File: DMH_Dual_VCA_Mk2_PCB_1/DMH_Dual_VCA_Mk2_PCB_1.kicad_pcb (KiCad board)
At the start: 2 copper layers, 48 x 175 mm, 70 parts, among them J1 TS_Jack_6.35mm_Sw, J100 IDC_02x05, J2 TS_Jack_6.35mm_Sw, J200 IDC_02x05, J3 TS_Jack_6.35mm_Sw, J4 TS_Jack_6.35mm_Sw, J5 TS_Jack_6.35mm_Sw, J50 Conn_01x08, J6 TS_Jack_6.35mm_Sw, J60 Conn_01x08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

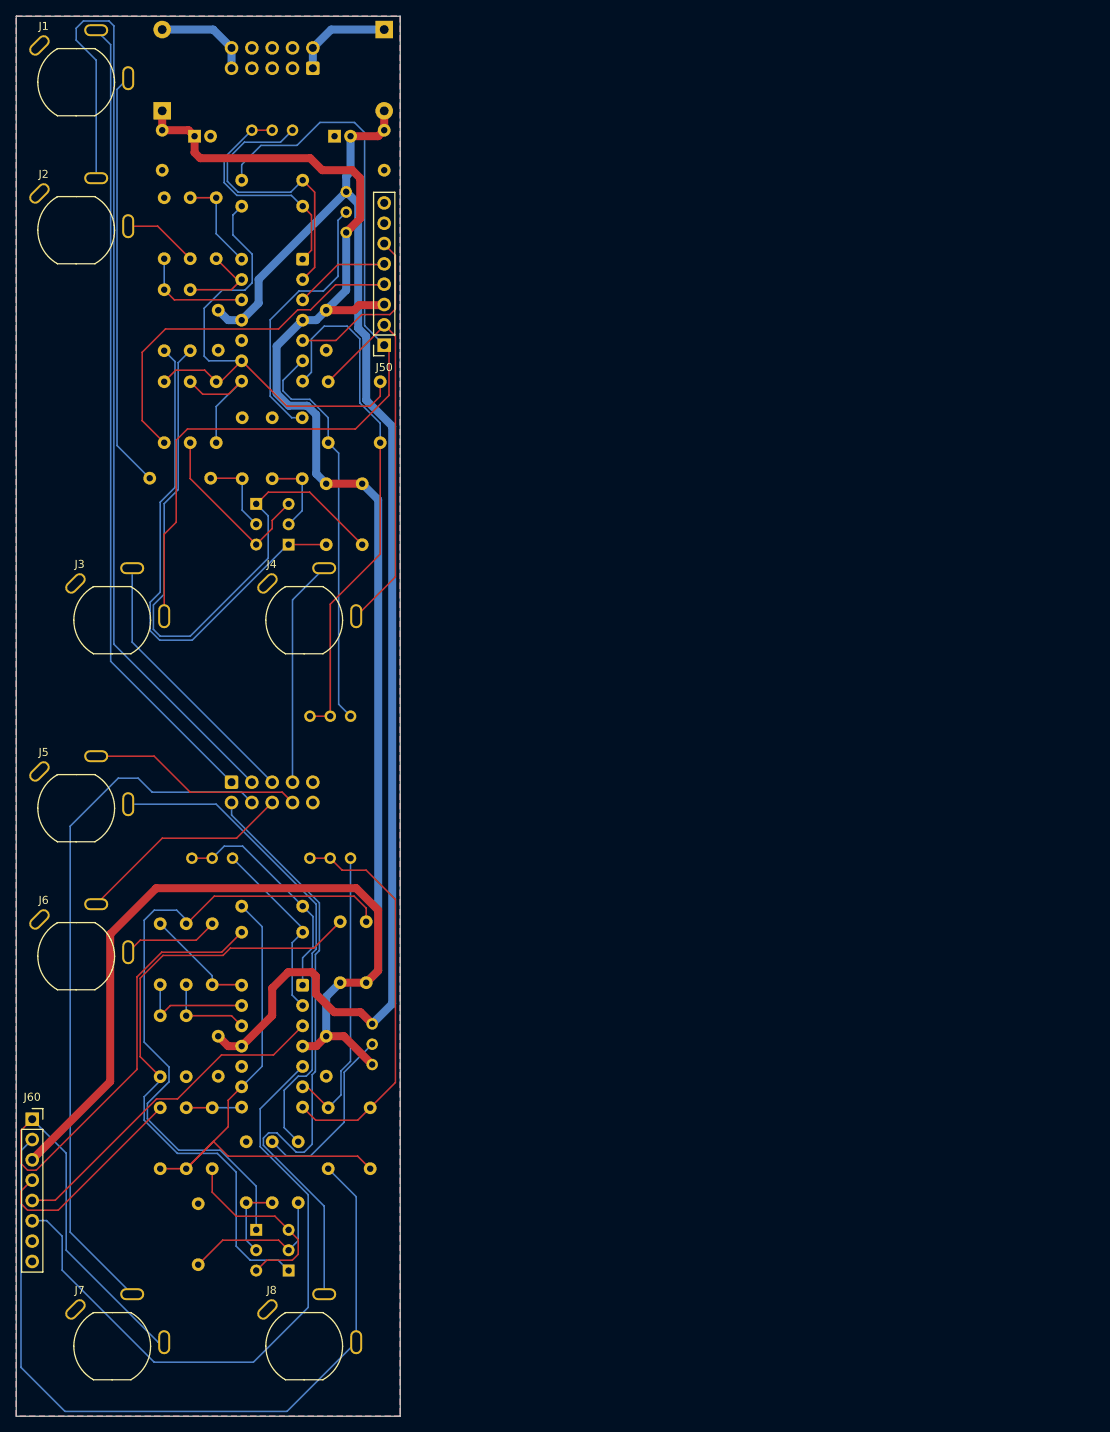
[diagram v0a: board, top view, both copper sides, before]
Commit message: Component placement ongoing on PCB1
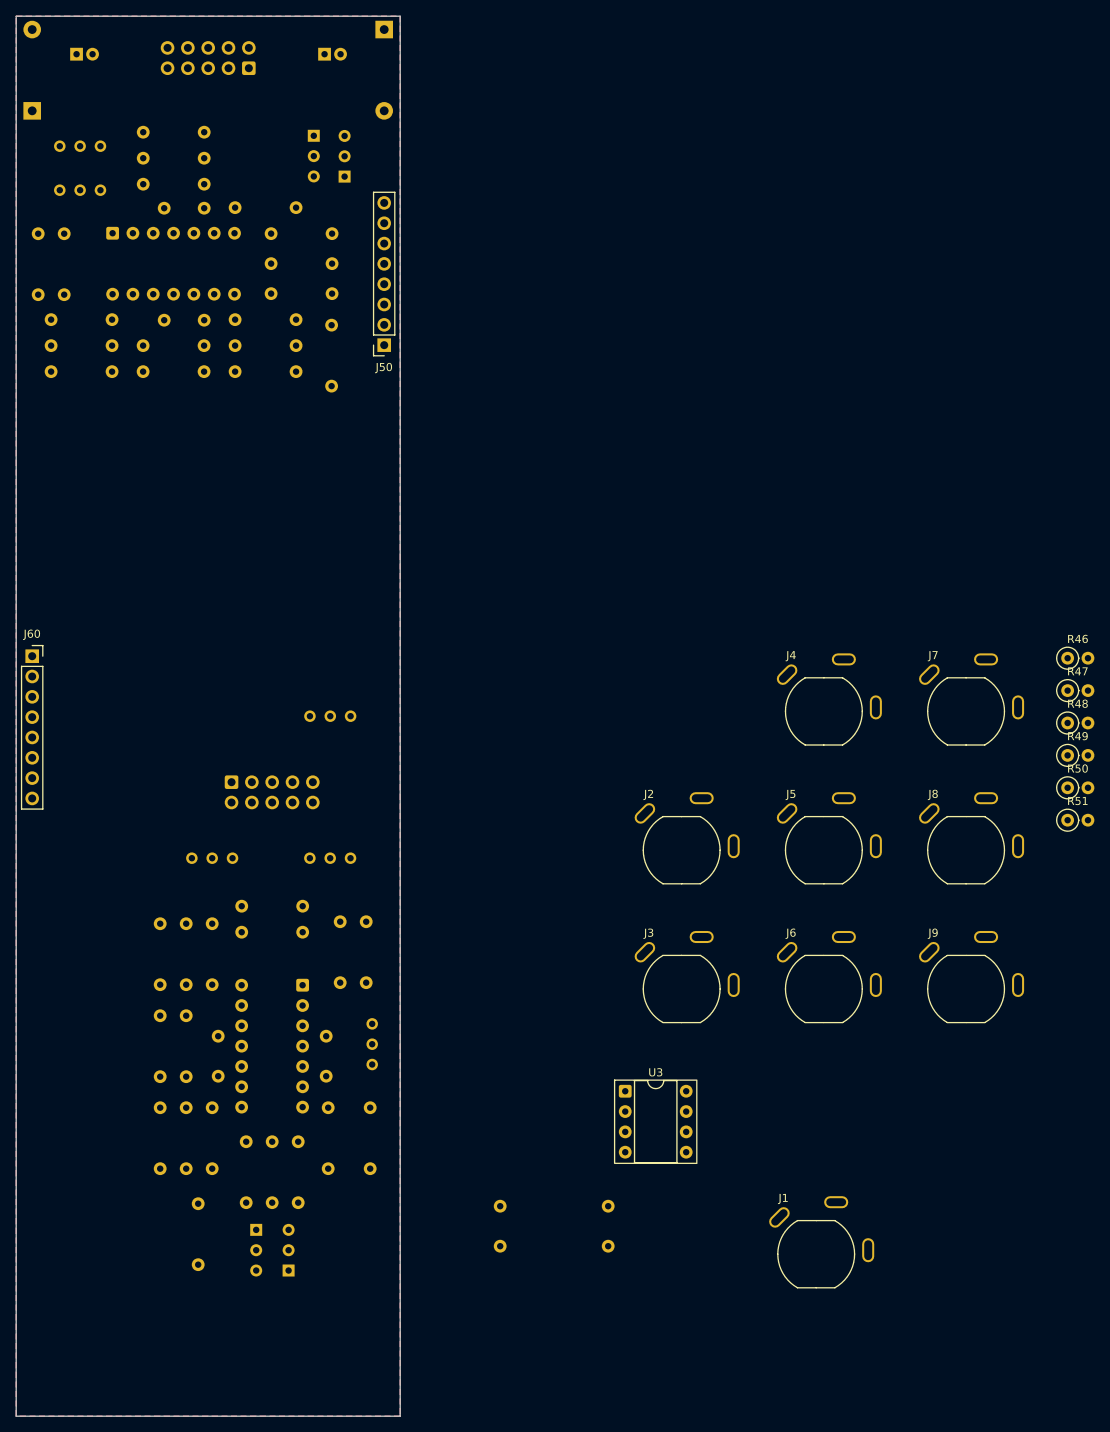
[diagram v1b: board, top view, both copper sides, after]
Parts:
- added J9: TS_Jack_6.35mm_Sw, SynthStuff:CUI_MJ-63052A, F.Cu at (169.7, 164.1)
- added R46: 100k, Resistor_THT:R_Axial_DIN0207_L6.3mm_D2.5mm_P2.54mm_Vertical, F.Cu at (182.4, 122.8)
- added R47: 100k, Resistor_THT:R_Axial_DIN0207_L6.3mm_D2.5mm_P2.54mm_Vertical, F.Cu at (182.4, 126.8)
- added R48: 100k, Resistor_THT:R_Axial_DIN0207_L6.3mm_D2.5mm_P2.54mm_Vertical, F.Cu at (182.4, 130.8)
- added R49: 100k, Resistor_THT:R_Axial_DIN0207_L6.3mm_D2.5mm_P2.54mm_Vertical, F.Cu at (182.4, 134.9)
- added R50: 100k, Resistor_THT:R_Axial_DIN0207_L6.3mm_D2.5mm_P2.54mm_Vertical, F.Cu at (182.4, 138.9)
- added R51: 1k, Resistor_THT:R_Axial_DIN0207_L6.3mm_D2.5mm_P2.54mm_Vertical, F.Cu at (182.4, 143.0)
- added U3: TL072, Package_DIP:DIP-8_W7.62mm_Socket, F.Cu at (127.1, 176.9)
- moved J1 173.3 mm to (151.0, 197.2)
- moved J7 133.0 mm to (169.7, 129.4)
- moved J2 108.3 mm to (134.2, 146.8)
- moved J8 103.4 mm to (169.7, 146.8)
- moved J5 93.6 mm to (152.0, 146.8)
- moved J6 93.5 mm to (152.0, 164.1)
- moved C5 90.8 mm to (89.8, 170.0)
- moved C6 90.8 mm to (76.2, 175.0)
- moved J3 84.8 mm to (134.2, 164.1)
- moved J4 66.0 mm to (152.0, 129.4)
- moved J60 57.9 mm to (53.0, 122.5)
- moved R15 50.7 mm to (74.5, 60.2), turned to 180 degrees
- moved R14 49.2 mm to (74.5, 63.5), turned to 180 degrees
- moved Q1 46.6 mm to (88.2, 57.5)
- moved Q2 46.5 mm to (92.0, 62.5)
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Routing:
- net +12V: track 254.4 -> 0.00 mm
- net -12V: track 176.0 -> 0.00 mm
- net Net-(J200-Pin_2): track 126.8 -> 0.00 mm
- net /Core Circuit A/CV 1 A Input: track 105.7 -> 0.00 mm
- net Net-(J200-Pin_1): track 101.0 -> 0.00 mm
- net /Core Circuit B/CV 2 B Input: track 100.0 -> 0.00 mm
- net /Core Circuit B/CV 1 B Input: track 88.3 -> 0.00 mm
- net Net-(J200-Pin_7): track 88.2 -> 0.00 mm
- net Net-(Q4-C): track 82.9 -> 0.00 mm
- net /Core Circuit B/CV 2 B Pot: track 82.0 -> 0.00 mm
- net Net-(Q1-C): track 79.5 -> 0.00 mm
- net Net-(Q3-C): track 79.0 -> 0.00 mm
- net Net-(J200-Pin_6): track 78.1 -> 0.00 mm
- net Net-(U2C--): track 66.9 -> 0.00 mm
- net Net-(R6-Pad1): track 66.4 -> 0.00 mm
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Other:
- board text added: "Mk2.0 - Month 2025"
- board text removed: "Mk1.0 - March 2025"

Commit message: Routed PCB 1
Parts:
- R46, R47, R48, R49, R50, R51: footprint Resistor_THT:R_Axial_DIN0207_L6.3mm_D2.5mm_P2.54mm_Vertical -> Resistor_THT:R_Axial_DIN0207_L6.3mm_D2.5mm_P7.62mm_Horizontal; moved to B.Cu
- U3: moved to B.Cu
- moved R46 126.2 mm to (57.5, 104.8), turned to 90 degrees
- moved R49 126.0 mm to (62.2, 97.2), turned to -90 degrees
- moved R48 121.4 mm to (66.9, 93.5)
- moved R51 118.5 mm to (68.8, 109.5), turned to 180 degrees
- moved R47 114.0 mm to (74.5, 90.2), turned to 180 degrees
- moved J7 112.6 mm to (75.0, 190.2)
- moved R50 106.1 mm to (80.5, 109.5), turned to 180 degrees
- moved C7 105.5 mm to (66.5, 103.5), turned to 90 degrees
- moved J2 97.8 mm to (58.5, 208.8), turned to -90 degrees
- moved U3 97.4 mm to (71.2, 97.2), turned to -90 degrees
- moved C8 96.9 mm to (83.5, 103.5)
- moved J1 96.0 mm to (58.5, 171.8), turned to -90 degrees
- moved J9 90.1 mm to (91.5, 208.8), turned to 90 degrees
- moved J8 89.5 mm to (91.5, 190.2), turned to 90 degrees
- moved J6 89.0 mm to (75.0, 208.8)
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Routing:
- net +12V: track 0.00 -> 189.3 mm
- net /Core Circuit A/CV 1 A Input: track 0.00 -> 174.0 mm
- net /Inputs and Outputs/Mix Out Jack: track 0.00 -> 171.6 mm
- net -12V: track 0.00 -> 167.1 mm
- net /Core Circuit A/Output A: track 0.00 -> 152.2 mm
- net /Core Circuit B/Output B: track 0.00 -> 144.5 mm
- net /Core Circuit A/CV 2 A Input: track 0.00 -> 121.4 mm
- net /Core Circuit B/CV 1 B Input: track 0.00 -> 108.0 mm
- net /Core Circuit B/CV 2 B Input: track 0.00 -> 106.1 mm
- net /Core Circuit A/Input A: track 0.00 -> 105.2 mm
- net Net-(Q2-C): track 0.00 -> 69.4 mm
- net Net-(U2C--): track 0.00 -> 67.8 mm
- net Net-(U1C--): track 0.00 -> 63.6 mm
- net Net-(J200-Pin_2): track 0.00 -> 60.5 mm
- net Net-(Q4-C): track 0.00 -> 58.6 mm
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
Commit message: Generated Gerbers
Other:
- board text added: "Mk2.0 - October 2025"
- board text removed: "Mk2.0 - Month 2025"
